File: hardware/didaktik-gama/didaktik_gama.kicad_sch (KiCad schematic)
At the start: 106 parts, among them J1 Klávesnice, J2 MG, J3 TV, J4 Porty 8255, SW1 RESET, T1 KSY72, T2 KSY72, T3 KC507, U1 UA880D (Z80), U10 4164, U11 4164, U12 4164, U13 4164, U14 4164, U15 4164, U16 4164, U17 2118, U18 2118, U19 2118, U2 27128 (16K EPROM), U20 2118, U21 2118, U22 2118, U23 2118, U24 2118, U25 74LS04, U26 74LS04, U27 74LS00, U28 74LS10, U29 74LS32, U3 8255 (MHB8255), U30 Kodér PAL, U31 Modulátor, U4 ULA, U5 74LS157, U6 74LS157, U7 74LS157, U8 74LS157, U9 4164, Y1 14MHz

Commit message: Add power supply section to Didaktik Gama schematic
Barrel jack, fuse, reverse-polarity diode, MA7805 regulator with input/
output filtering, power LED, and 100n decoupling on every IC plus bulk
caps for the DRAM banks. Marked as added (not on the original).

Co-Authored-By: Claude Opus 5.5 <noreply@anthropic.com>
Claude-Session: https://claude.ai/code/session_01LAVM7Gq9EYiUXiCEdy9ZRx
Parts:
- added C11: 1000u/25V, Capacitor_THT:CP_Radial_D10.0mm_P5.00mm, symbol gama:CP
- added C12, C13, C20, C21, C22, C23, C24, C25, C26, C27, C28, C29, C30, C31, C32, C33, C34, C35, C36, C37, C38, C39, C40, C41, C42, C43, C44, C45, C46, C47, C48: 100n, Capacitor_THT:C_Disc_D5.0mm_W2.5mm_P5.00mm, symbol gama:C
- added C14: 220u/10V, Capacitor_THT:CP_Radial_D6.3mm_P2.50mm, symbol gama:CP
- added C15: 10u/16V, Capacitor_THT:CP_Radial_D5.0mm_P2.00mm, symbol gama:CP
- added C60, C61: 47u/10V, Capacitor_THT:CP_Radial_D5.0mm_P2.00mm, symbol gama:CP
- added D12: KY132/80 (1N4007), Diode_THT:D_DO-41_SOD81_P10.16mm_Horizontal, symbol gama:D
- added D13: LED zelená, LED_THT:LED_D5.0mm, symbol gama:LED
- added F1: 1A T, Fuse:Fuseholder_Cylinder-5x20mm_Stelvio-Kontek_PTF78_Horizontal_Open, symbol gama:F
- added J5: Napájení 9–12V DC, Connector_BarrelJack:BarrelJack_Horizontal, symbol gama:CONN_2
- added R45: 470, Resistor_THT:R_Axial_DIN0207_L6.3mm_D2.5mm_P10.16mm_Horizontal, symbol gama:R
- added U32: MA7805, Package_TO_SOT_THT:TO-220-3_Vertical, symbol gama:7805
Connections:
- net +5V: now also C13.1, C14.1, C15.1, C20.1, C21.1, C22.1, C23.1, C24.1, C25.1, C26.1, C27.1, C28.1, C29.1, C30.1, C31.1, C32.1, C33.1, C34.1, C35.1, C36.1, C37.1, C38.1, C39.1, C40.1, C41.1, C42.1, C43.1, C44.1, C45.1, C46.1, C47.1, C48.1, C60.1, C61.1, D13.2, U32.3 (OUT)
- net GND: now also C11.2, C12.2, C13.2, C14.2, C15.2, C20.2, C21.2, C22.2, C23.2, C24.2, C25.2, C26.2, C27.2, C28.2, C29.2, C30.2, C31.2, C32.2, C33.2, C34.2, C35.2, C36.2, C37.2, C38.2, C39.2, C40.2, C41.2, C42.2, C43.2, C44.2, C45.2, C46.2, C47.2, C48.2, C60.2, C61.2, J5.2, R45.2, U32.2 (GND)
- new net LED_K: D13.1, R45.1
- new net VIN: C11.1, C12.1, D12.1, U32.1 (IN)
- new net VIN_F: D12.2, F1.2
- new net VIN_RAW: F1.1, J5.1
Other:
- note added: "NAPÁJENÍ (doplněno – na předloze jen +5V)"
- note added: "• C20–C61: blokování napájení – Doplněno: 100n u každého IC (u napájecích pinů), 47u u bank 4164 a 2118"
- note added: "• Napájení (J5, F1, D12, U32): celý blok doplněn – Na předloze není – vstupní napětí 9–12 V DC a hodnoty kondenzátorů jsou typické pro 7805, ověřit na desce/adaptéru"
- moved on the sheet: C1, C10, C2, C3, C4, C5, C6, C7, C8, C9, D1, D10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

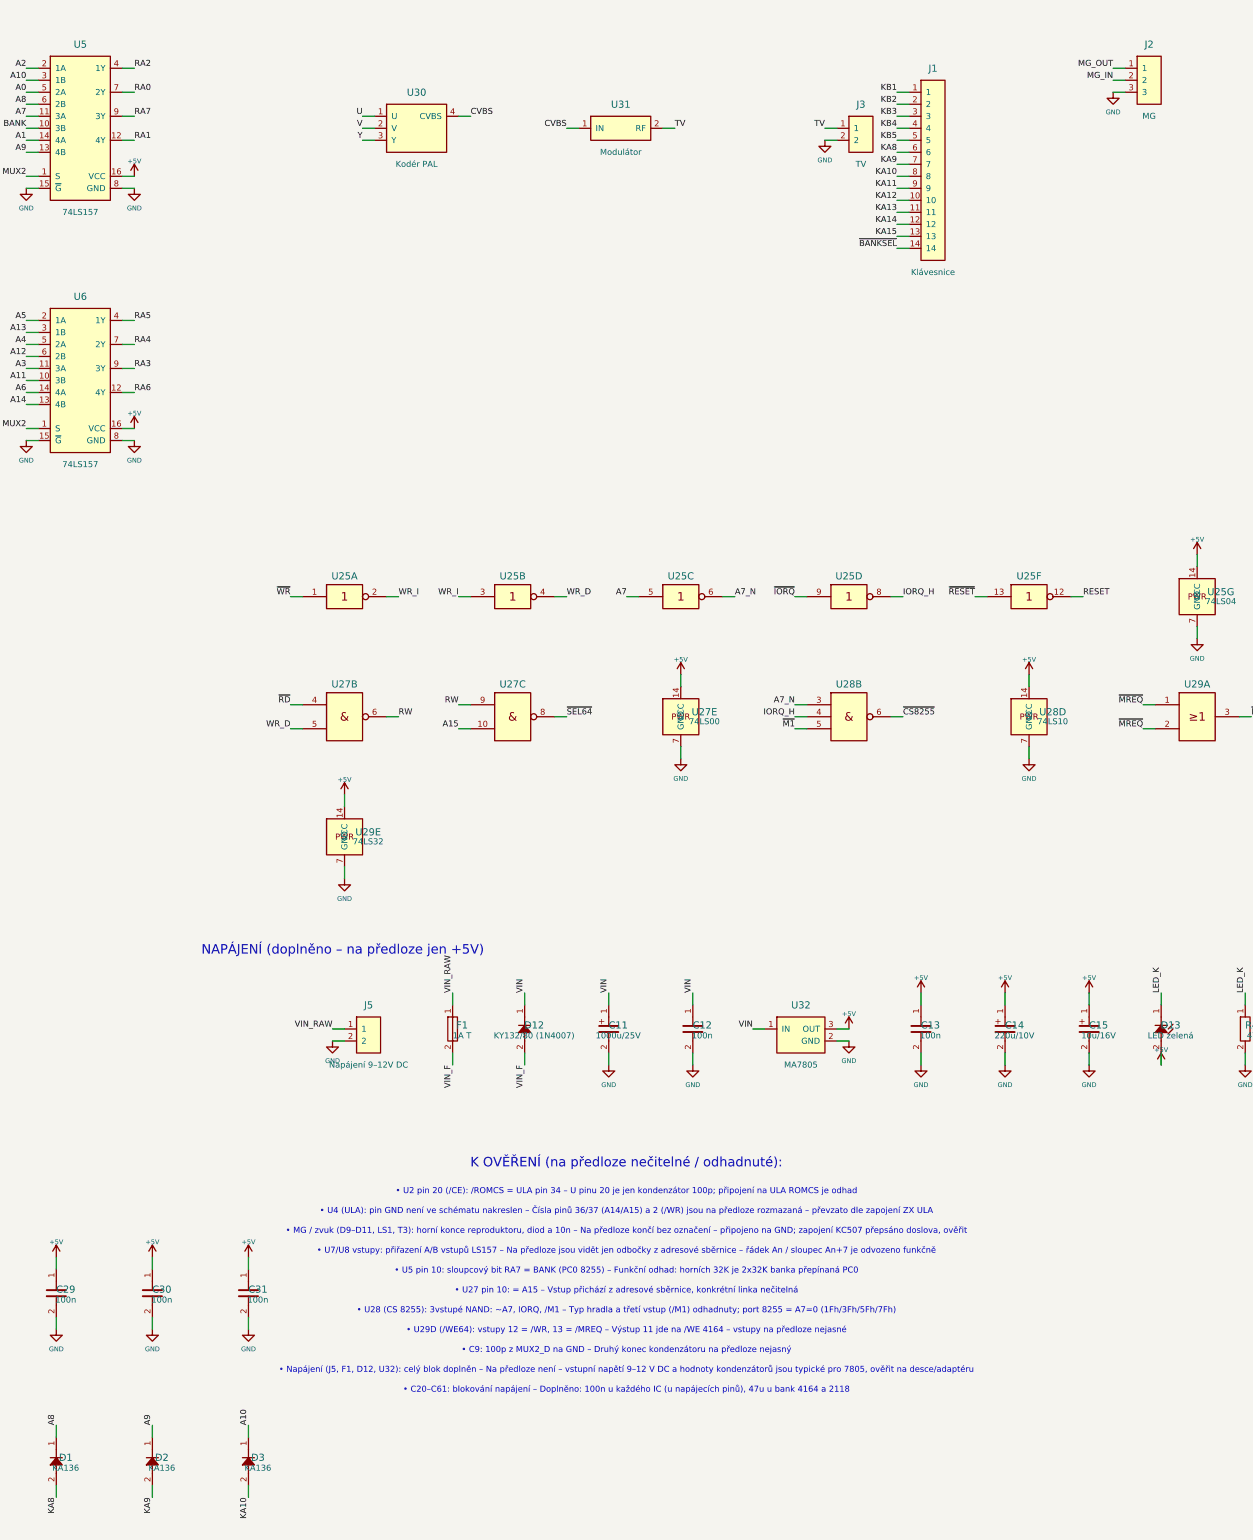
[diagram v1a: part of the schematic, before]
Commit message: Add composite video output and modulator pins to Didaktik Gama schematic
Emitter-follower CVBS output to RCA jack, modulator module with supply
and RF pins; coder kept as a block pending datasheet verification.

Co-Authored-By: Claude Opus 5.5 <noreply@anthropic.com>
Claude-Session: https://claude.ai/code/session_01LAVM7Gq9EYiUXiCEdy9ZRx
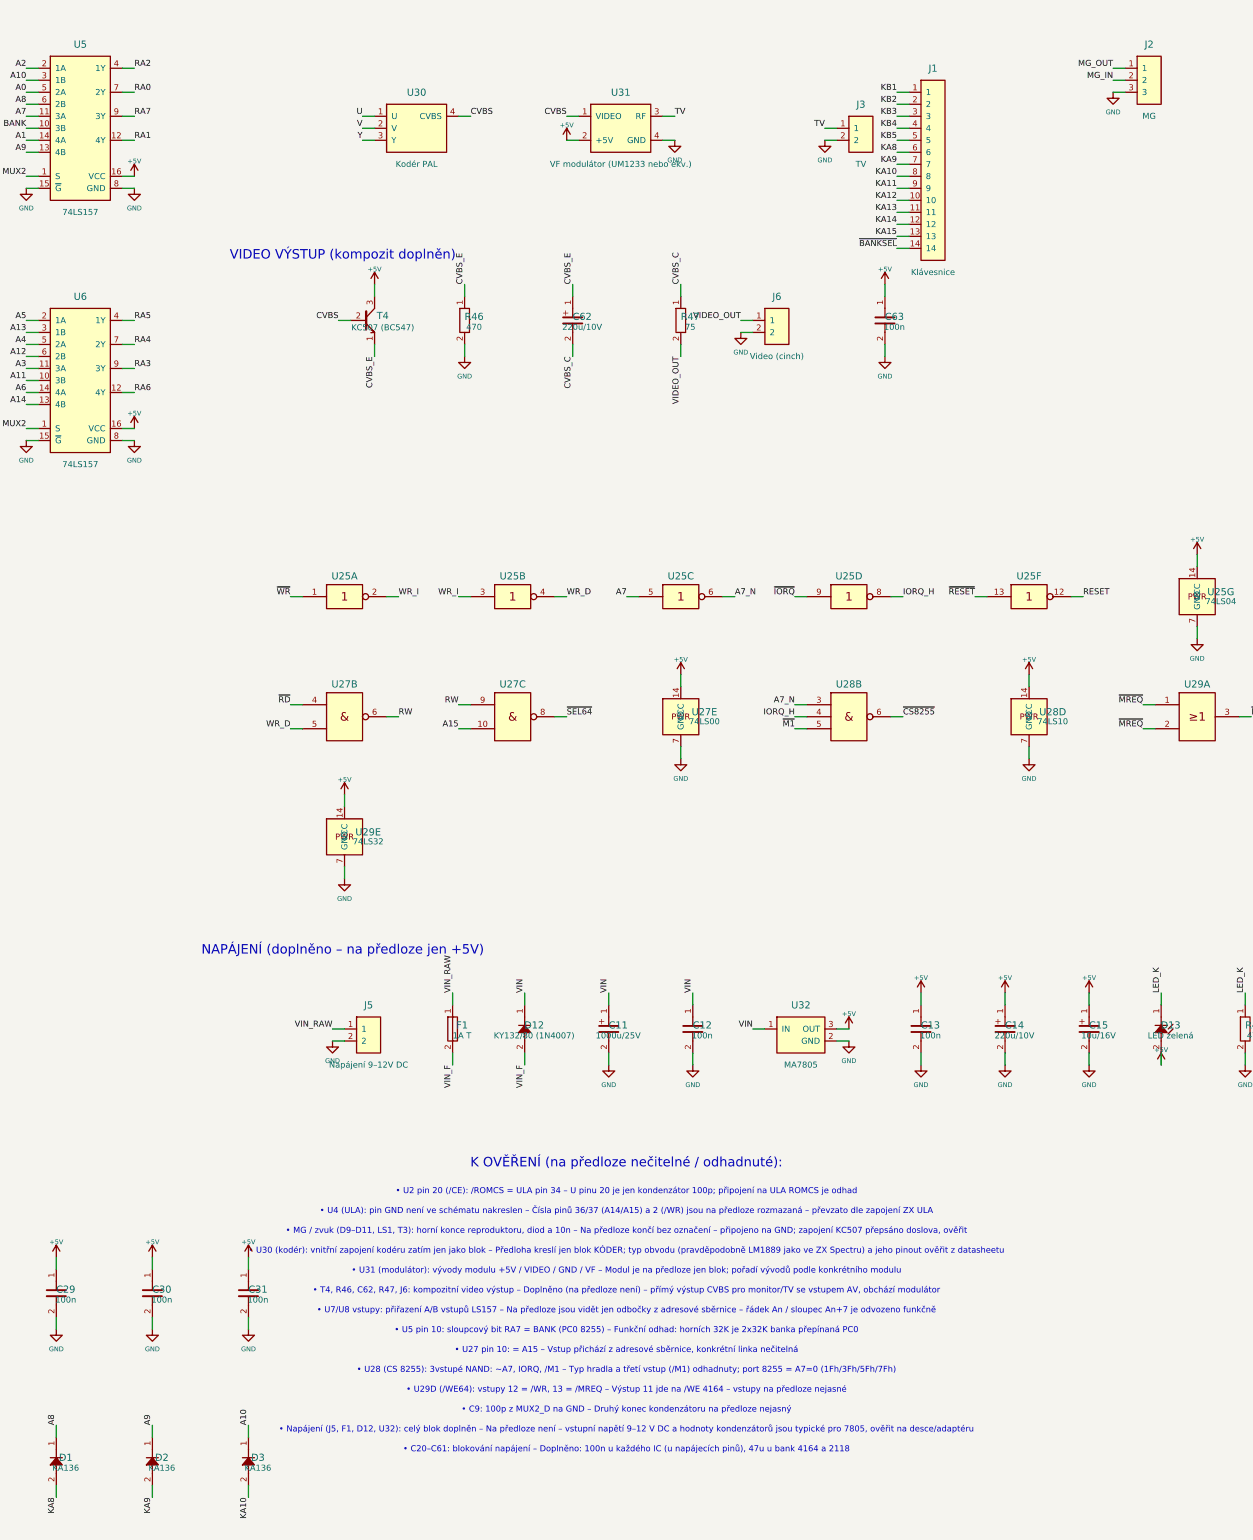
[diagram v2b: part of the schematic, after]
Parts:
- removed unit 1 of U25
- removed unit 5 of U26
- removed unit 3 of U29
- added C10: 100p, Capacitor_THT:C_Disc_D5.0mm_W2.5mm_P5.00mm, symbol gama:C
- added C62: 220u/10V, Capacitor_THT:CP_Radial_D6.3mm_P2.50mm, symbol gama:CP
- added C63: 100n, Capacitor_THT:C_Disc_D5.0mm_W2.5mm_P5.00mm, symbol gama:C
- added J6: Video (cinch), Connector_Coaxial:CONN_RCA_Horizontal, symbol gama:CONN_2
- added R43: 220, Resistor_THT:R_Axial_DIN0207_L6.3mm_D2.5mm_P10.16mm_Horizontal, symbol gama:R
- added R46: 470, Resistor_THT:R_Axial_DIN0207_L6.3mm_D2.5mm_P10.16mm_Horizontal, symbol gama:R
- added R47: 75, Resistor_THT:R_Axial_DIN0207_L6.3mm_D2.5mm_P10.16mm_Horizontal, symbol gama:R
- added T4: KC507 (BC547), Package_TO_SOT_THT:TO-18-3, symbol gama:NPN
- added unit 7 of U26
- U26: renamed from U28; value 74LS10 -> 74LS04; symbol gama:7410 -> gama:7404
- U28: renamed from R43; value 220 -> 74LS10; footprint Resistor_THT:R_Axial_DIN0207_L6.3mm_D2.5mm_P10.16mm_Horizontal -> Package_DIP:DIP-14_W7.62mm; symbol gama:R -> gama:7410
- U29: renamed from C10; value 100p -> 74LS32; footprint Capacitor_THT:C_Disc_D5.0mm_W2.5mm_P5.00mm -> Package_DIP:DIP-14_W7.62mm; symbol gama:C -> gama:7432
- U31: value Modulátor -> VF modulátor (UM1233 nebo ekv.)
- renumbered U26 to U25
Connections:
- net +5V: now also U28.14 (VCC), U31.2 (+5V), C63.1, T4.3 (C), U26.14 (VCC); no longer U25.14 (VCC), U26.14 (VCC)
- net BANK: now also U26.11
- net CVBS: now also T4.2 (B)
- net GND: now also U28.7 (GND), U31.4 (GND), C10.2, C63.2, J6.2, R46.2, U26.7 (GND); no longer U25.7 (GND), U26.7 (GND), U29.2
- net MUX2: now also U29.8
- net RAS_D: now also U29.9, R43.2; no longer U28.2
- net TV: now also U31.3 (RF); no longer U31.2 (RF)
- net WR_I: now also U25.2
- net ~{BANKSEL}: now also U26.10
- net ~{MREQ}: now also C10.1; no longer U29.1
- net ~{RAS64}: now also R43.1; no longer U28.1
- net ~{SEL64}: now also U29.10
- net ~{WR}: now also U25.1
- new net CVBS_C: C62.2, R47.1
- new net CVBS_E: C62.1, R46.1, T4.1 (E)
- new net VIDEO_OUT: J6.1, R47.2
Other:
- note added: "VIDEO VÝSTUP (kompozit doplněn)"
- note added: "• T4, R46, C62, R47, J6: kompozitní video výstup – Doplněno (na předloze není) – přímý výstup CVBS pro monitor/TV se vstupem AV, obchází modulátor"
- note added: "• U30 (kodér): vnitřní zapojení kodéru zatím jen jako blok – Předloha kreslí jen blok KÓDER; typ obvodu (pravděpodobně LM1889 jako ve ZX Spectru) a jeho pinout ověřit z datasheetu"
- note added: "• U31 (modulátor): vývody modulu +5V / VIDEO / GND / VF – Modul je na předloze jen blok; pořadí vývodů podle konkrétního modulu"

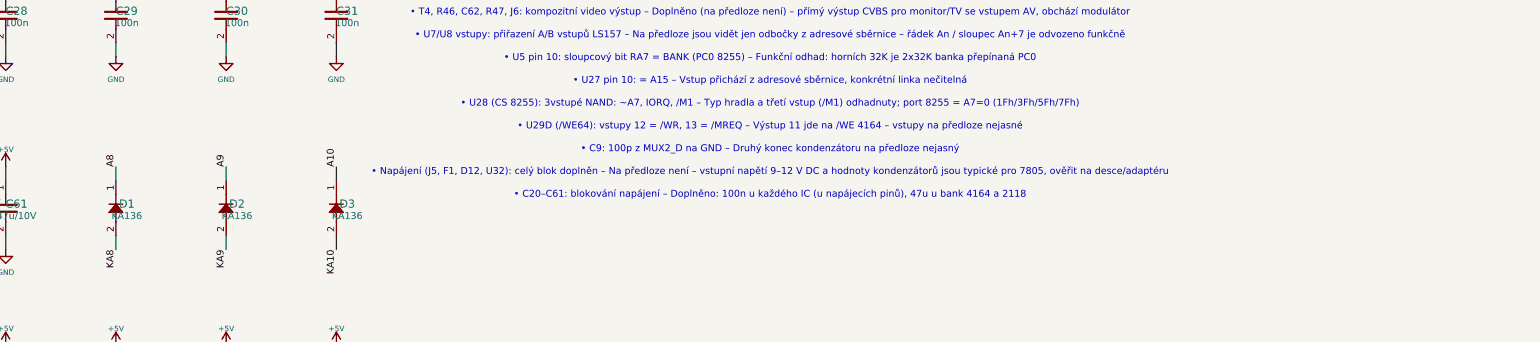
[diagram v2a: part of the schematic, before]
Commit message: Note Spectrum 128 service manual as reference for the power supply
Co-Authored-By: Claude Opus 5.5 <noreply@anthropic.com>
Claude-Session: https://claude.ai/code/session_01LAVM7Gq9EYiUXiCEdy9ZRx
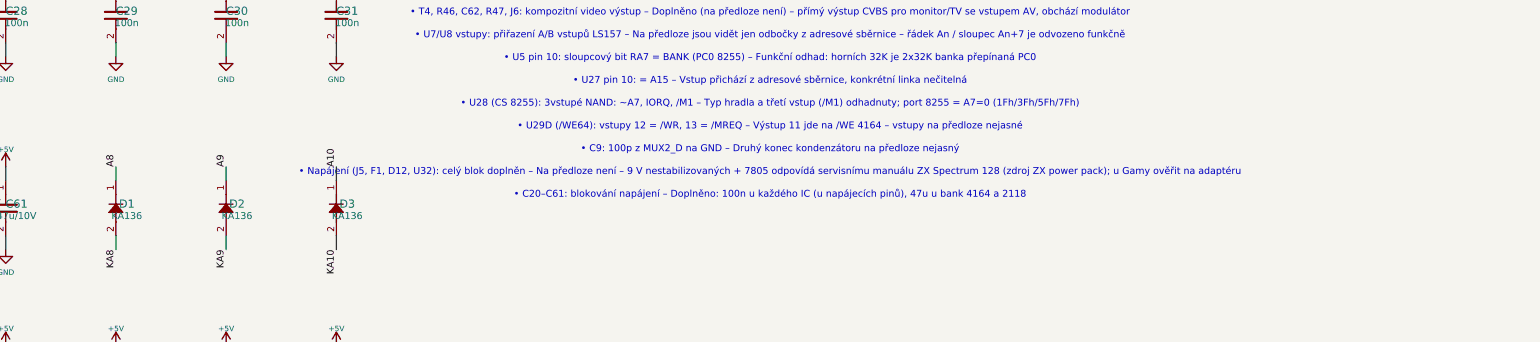
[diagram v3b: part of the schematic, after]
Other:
- note added: "• Napájení (J5, F1, D12, U32): celý blok doplněn – Na předloze není – 9 V nestabilizovaných + 7805 odpovídá servisnímu manuálu ZX Spectrum 128 (zdroj ZX power pack); u Gamy ověřit na adaptéru"
- note removed: "• Napájení (J5, F1, D12, U32): celý blok doplněn – Na předloze není – vstupní napětí 9–12 V DC a hodnoty kondenzátorů jsou typické pro 7805, ověřit na desce/adaptéru"
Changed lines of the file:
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@@
         (size 1.27 1.27)))
 )
-  (text "• Napájení (J5, F1, D12, U32): celý blok doplněn – Na předloze není – vstupní napětí 9–12 V DC a hodnoty kondenzátorů jsou typické pro 7805, ověřit na desce/adaptéru"
+  (text "• Napájení (J5, F1, D12, U32): celý blok doplněn – Na předloze není – 9 V nestabilizovaných + 7805 odpovídá servisnímu manuálu ZX Spectrum 128 (zdroj ZX power pack); u Gamy ověřit na adaptéru"
     (at 560.00 346.40 0)
     (effects

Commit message: Draw LM1889 PAL coder circuit in Didaktik Gama schematic
Pin functions from the ZX Spectrum 48K service manual (IC14 pin table):
U/V level shift with trimmers, 4.433619 MHz oscillator with lead/lag RC,
luma/chroma summing transistors to CVBS, +12V feed for the coder.
Uncertain values listed in k_overeni.csv.

Co-Authored-By: Claude Opus 5.5 <noreply@anthropic.com>
Claude-Session: https://claude.ai/code/session_01LAVM7Gq9EYiUXiCEdy9ZRx
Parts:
- removed D12: KY132/80 (1N4007), Diode_THT:D_DO-41_SOD81_P10.16mm_Horizontal, symbol gama:D
- removed J4: Porty 8255, Connector_PinHeader_2.54mm:PinHeader_2x13_P2.54mm_Vertical, symbol gama:CONN_26
- removed U16: 4164, Package_DIP:DIP-16_W7.62mm, symbol gama:4164
- removed U21: 2118, Package_DIP:DIP-16_W7.62mm, symbol gama:2118
- removed unit 3 of U29
- removed U30: Kodér PAL, symbol gama:KODER
- added C24, C32, C64, C70: 100n, Capacitor_THT:C_Disc_D5.0mm_W2.5mm_P5.00mm, symbol gama:C
- added C65: 5–30p trimr (TC2), Capacitor_THT:C_Disc_D5.0mm_W2.5mm_P5.00mm, symbol gama:C
- added C66, C67: 150p, Capacitor_THT:C_Disc_D5.0mm_W2.5mm_P5.00mm, symbol gama:C
- added C69: 100u/16V, Capacitor_THT:CP_Radial_D6.3mm_P2.50mm, symbol gama:CP
- added R19: 470, Resistor_THT:R_Axial_DIN0207_L6.3mm_D2.5mm_P10.16mm_Horizontal, symbol gama:R
- added R48, R50, R52, R53, R55, R56: 1k, Resistor_THT:R_Axial_DIN0207_L6.3mm_D2.5mm_P10.16mm_Horizontal, symbol gama:R
- added R49: 2k2 trimr (VR1), Resistor_THT:R_Axial_DIN0207_L6.3mm_D2.5mm_P10.16mm_Horizontal, symbol gama:R
- added R51: 2k2 trimr (VR2), Resistor_THT:R_Axial_DIN0207_L6.3mm_D2.5mm_P10.16mm_Horizontal, symbol gama:R
- added R54: 100, Resistor_THT:R_Axial_DIN0207_L6.3mm_D2.5mm_P10.16mm_Horizontal, symbol gama:R
- added R57: 47, Resistor_THT:R_Axial_DIN0207_L6.3mm_D2.5mm_P10.16mm_Horizontal, symbol gama:R
- added T5, T6: KC507 (ZTX313), Package_TO_SOT_THT:TO-18-3, symbol gama:NPN
- added U18: 2118, Package_DIP:DIP-16_W7.62mm, symbol gama:2118
- added unit 5 of U27
- added U30: LM1889, Package_DIP:DIP-18_W7.62mm, symbol gama:LM1889
- added U32: MA7805, Package_TO_SOT_THT:TO-220-3_Vertical, symbol gama:7805
- added Y2: 4.433619MHz, Crystal:Crystal_HC49-4H_Vertical, symbol gama:XTAL
- C68: renamed from U18; value 2118 -> 1n; footprint Package_DIP:DIP-16_W7.62mm -> Capacitor_THT:C_Disc_D5.0mm_W2.5mm_P5.00mm; symbol gama:2118 -> gama:C
- D12: renamed from C32; value 100n -> KY132/80 (1N4007); footprint Capacitor_THT:C_Disc_D5.0mm_W2.5mm_P5.00mm -> Diode_THT:D_DO-41_SOD81_P10.16mm_Horizontal; symbol gama:C -> gama:D
- J4: renamed from C24; value 100n -> Porty 8255; footprint Capacitor_THT:C_Disc_D5.0mm_W2.5mm_P5.00mm -> Connector_PinHeader_2.54mm:PinHeader_2x13_P2.54mm_Vertical; symbol gama:C -> gama:CONN_26
- U16: renamed from U27; value 74LS00 -> 4164; footprint Package_DIP:DIP-14_W7.62mm -> Package_DIP:DIP-16_W7.62mm; symbol gama:7400 -> gama:4164
- U21: renamed from R19; value 470 -> 2118; footprint Resistor_THT:R_Axial_DIN0207_L6.3mm_D2.5mm_P10.16mm_Horizontal -> Package_DIP:DIP-16_W7.62mm; symbol gama:R -> gama:2118
- U29: renamed from U32; value MA7805 -> 74LS32; footprint Package_TO_SOT_THT:TO-220-3_Vertical -> Package_DIP:DIP-14_W7.62mm; symbol gama:7805 -> gama:7432
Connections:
- net +5V: now also J4.25, U16.8 (VCC), U21.8 (VCC), U21.9 (VCC), C24.1, C32.1, R55.1, T6.3 (C), U18.8 (VCC), U18.9 (VCC), U27.14 (VCC), U32.3 (OUT); no longer C68.8 (VCC), C68.9 (VCC), D12.1, J4.1, U16.14 (VCC), U29.3 (OUT)
- net CVBS: now also R56.1, T6.1 (E)
- net D0: now also R19.1; no longer U21.1
- net D7: now also U16.14 (Q), U16.2 (D)
- net GND: now also J4.26, U16.16 (GND), U21.16 (GND), C24.2, C32.2, C64.2, C65.2, C67.2, C69.2, C70.2, R54.2, R56.2, U18.16 (GND), U27.7 (GND), U30.5 (GND), U32.2 (GND); no longer C68.16 (GND), D12.2, J4.2, U16.7 (GND), U29.2 (GND)
- net MUX2: now also U29.8
- net PA0: now also J4.1
- net PA1: now also J4.2
- net PA2: now also J4.3
- net PA3: now also J4.4
- net PA4: now also J4.5
- net PA5: now also J4.6
- net PA6: now also J4.7
- net PA7: now also J4.8
- net PB0: now also J4.9
- net PB1: now also J4.10
- net PB2: now also J4.11
- net PB3: now also J4.12
- net PB4: now also J4.13
- net PB5: now also J4.14
- net PB6: now also J4.15
- net PB7: now also J4.16
- net PC0: now also J4.17
- net PC1: now also J4.18
- net PC2: now also J4.19
- net PC3: now also J4.20
- net PC4: now also J4.21
- net PC5: now also J4.22
- net PC6: now also J4.23
- net PC7: now also J4.24
- net RA0: now also U16.5 (A0)
- net RA1: now also U16.7 (A1)
- net RA2: now also U16.6 (A2)
- net RA3: now also U16.12 (A3)
- net RA4: now also U16.11 (A4)
- net RA5: now also U16.10 (A5)
- net RA6: now also U16.13 (A6)
- net RA7: now also U16.9 (A7)
- net RAS_D: now also U29.9
- net U: now also R48.1
- net V: now also R50.1
- net VA0: now also U21.5 (A0), U18.5 (A0); no longer C68.5 (A0)
- net VA1: now also U21.11 (A4), U18.11 (A4); no longer C68.11 (A4)
- net VA2: now also U21.7 (A1), U18.7 (A1); no longer C68.7 (A1)
- net VA3: now also U21.13 (A6), U18.13 (A6); no longer C68.13 (A6)
- net VA4: now also U21.12 (A3), U18.12 (A3); no longer C68.12 (A3)
- net VA5: now also U21.10 (A5), U18.10 (A5); no longer C68.10 (A5)
- net VA6: now also U21.6 (A2), U18.6 (A2); no longer C68.6 (A2)
- net VD0: now also R19.2; no longer U21.2
- net VD1: now also U18.14 (Q), U18.2 (D); no longer C68.14 (Q), C68.2 (D)
- net VD4: now also U21.14 (Q), U21.2 (D)
- net VIN: now also D12.1, R57.1, U32.1 (IN); no longer U29.1 (IN)
- net VIN_F: now also D12.2
- net Y: now also R53.1
- net ~{CAS64}: now also U16.15 (~{CAS})
- net ~{RAS64}: now also U16.4 (~{RAS})
- net ~{SEL64}: now also U29.10
- net ~{VCAS}: now also U21.15 (~{CAS}), U18.15 (~{CAS}); no longer C68.15 (~{CAS})
- net ~{VRAS}: now also U21.4 (~{RAS}), U18.4 (~{RAS}); no longer C68.4 (~{RAS})
- net ~{VWE}: now also U21.3 (~{WE}), U18.3 (~{WE}); no longer C68.3 (~{WE})
- net ~{WE64}: now also U16.3 (~{WE})
- net CHROMA: now reaches C68.1
- net CHROMA: now also U30.13 (CHROMA)
- new net +12V: C69.1, C70.1, R57.2, U30.12 (VIDEO), U30.14 (RF_VCC), U30.15 (SND), U30.16 (VCC)
- new net BY: R48.2, R49.1, U30.4 (B-Y)
- new net CBIAS: C64.1, R49.2, R51.2, U30.3 (BIAS)
- new net CH_LAG: C66.2, C67.1, U30.18 (LAG)
- new net CH_LEAD: C66.1, R52.2, U30.1 (LEAD)
- new net CH_OSC: R52.1, U30.17 (OSC), Y2.1
- new net CH_XT: C65.1, Y2.2
- new net CVBS_MIX: C68.2, R55.2, T5.3 (C), T6.2 (B)
- new net RY: R50.2, R51.1, U30.2 (R-Y)
- new net T5_B: R53.2, T5.2 (B)
- new net T5_E: R54.1, T5.1 (E)
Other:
- note added: "KODÉR PAL LM1889 + VIDEO VÝSTUP"
- note added: "• R48–R51, C64: posun úrovně U/V (trimry VR1/VR2 2k2) – Topologie podle popisu v manuálu (Issue 2), hodnoty 1k typické – nastavit dle kap. 3.1.3 manuálu"
- note added: "• R57, C69 (+12V): napájení LM1889 z nestabilizovaného vstupu – Spectrum vyrábí +12 V měničem TR4/TR5; u Gamy zdroj 12 V ověřit (při 9V adaptéru nestačí)"
- note added: "• T5, T6, R53–R56, C68: sčítání jasu a barvy do CVBS – Podle popisu v manuálu (TR1/TR2 ZTX313); hodnoty typické, ověřit"
- note added: "• U30 LM1889: piny podle servisního manuálu ZX Spectrum 48K (kap. 7.1) – Typ kodéru u Gamy ověřit na desce; piny 12/14/15 na +12V podle tabulky napětí v manuálu"
- note added: "• Y2, C65–C67, R52: oscilátor 4,433619 MHz a fázovací RC 1–18 – Krystal a 150p dle soupisu Spectra; přesné zapojení RC článku ze schématu Spectra ověřit"
- note removed: "VIDEO VÝSTUP (kompozit doplněn)"
- note removed: "• U30 (kodér): vnitřní zapojení kodéru zatím jen jako blok – Předloha kreslí jen blok KÓDER; typ obvodu (pravděpodobně LM1889 jako ve ZX Spectru) a jeho pinout ověřit z datasheetu"
- moved on the sheet: D12
